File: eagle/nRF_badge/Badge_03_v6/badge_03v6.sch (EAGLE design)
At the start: 45 parts, among them J1 PROG_CONN_6, U1 LIS2DH12, U2 LP2985LV, U3 MCP6231, U5 M95M02, Y1 32768Hz

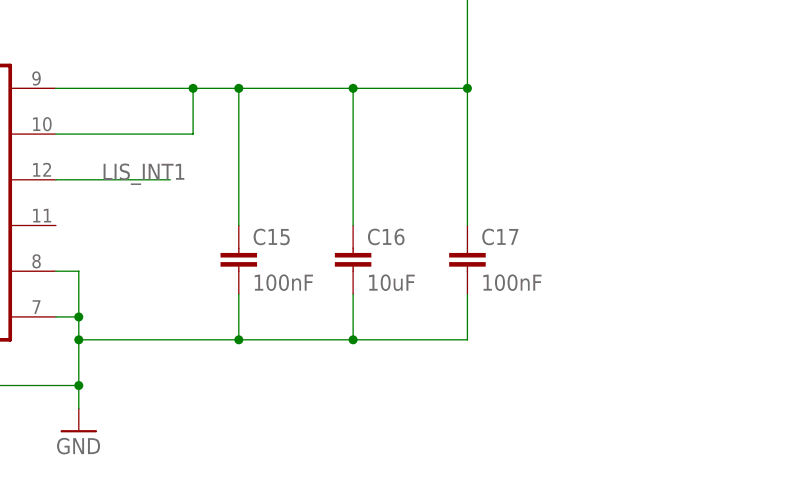
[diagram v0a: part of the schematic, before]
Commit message: Adding an accelerometer
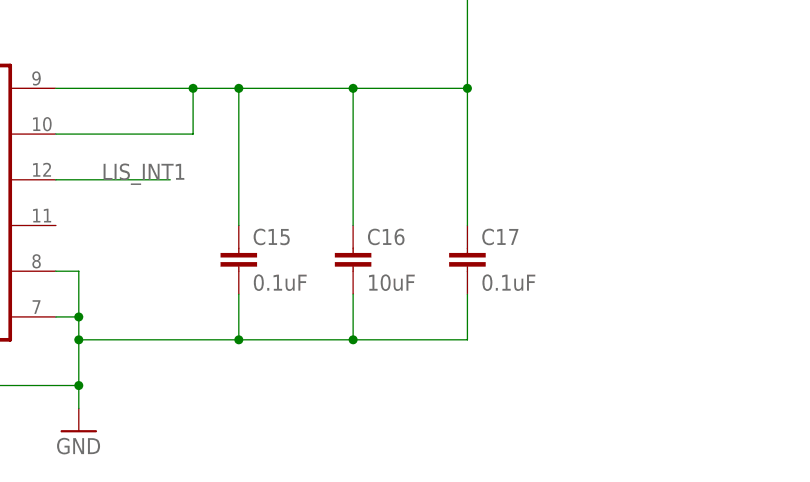
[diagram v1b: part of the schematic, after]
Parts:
- C15, C17: value 100nF -> 0.1uF
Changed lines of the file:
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@@
 <part name="GND9" library="Badge" deviceset="GND" device=""/>
 <part name="SUPPLY3" library="Badge" deviceset="VCC" device=""/>
-<part name="C15" library="rcl" deviceset="C-EU" device="C0603" value="100nF"/>
+<part name="C15" library="rcl" deviceset="C-EU" device="C0603" value="0.1uF"/>
 <part name="C16" library="rcl" deviceset="C-EU" device="C0603" value="10uF"/>
-<part name="C17" library="rcl" deviceset="C-EU" device="C0603" value="100nF"/>
+<part name="C17" library="rcl" deviceset="C-EU" device="C0603" value="0.1uF"/>
 <part name="SUPPLY18" library="Badge" deviceset="VCC" device=""/>
 <part name="SUPPLY19" library="Badge" deviceset="VCC" device=""/>

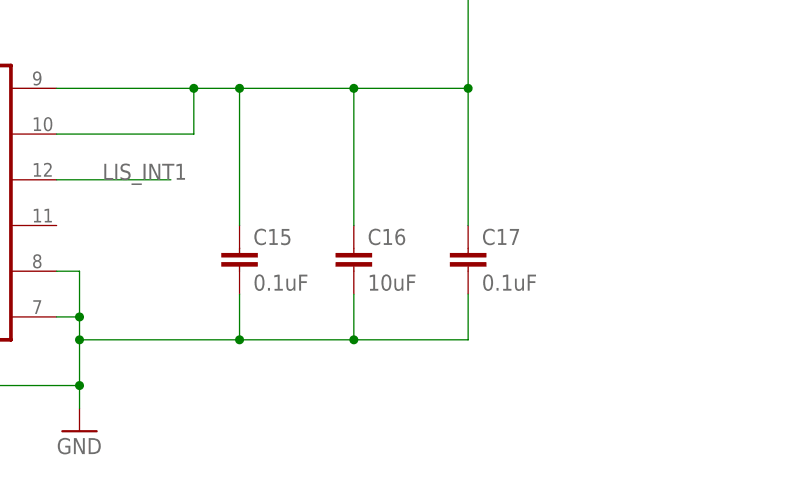
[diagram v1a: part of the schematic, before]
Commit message: Cleanning up labels
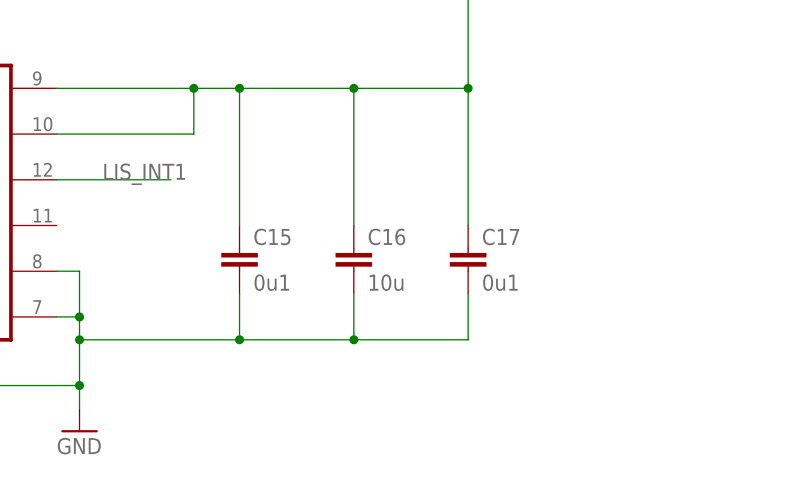
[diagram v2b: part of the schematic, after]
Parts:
- C15, C17: value 0.1uF -> 0u1
- C16: value 10uF -> 10u
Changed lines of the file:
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@@
 <part name="GND9" library="Badge" deviceset="GND" device=""/>
 <part name="SUPPLY3" library="Badge" deviceset="VCC" device=""/>
-<part name="C15" library="rcl" deviceset="C-EU" device="C0603" value="0.1uF"/>
-<part name="C16" library="rcl" deviceset="C-EU" device="C0603" value="10uF"/>
-<part name="C17" library="rcl" deviceset="C-EU" device="C0603" value="0.1uF"/>
+<part name="C15" library="rcl" deviceset="C-EU" device="C0603" value="0u1"/>
+<part name="C16" library="rcl" deviceset="C-EU" device="C0603" value="10u"/>
+<part name="C17" library="rcl" deviceset="C-EU" device="C0603" value="0u1"/>
 <part name="SUPPLY18" library="Badge" deviceset="VCC" device=""/>
 <part name="SUPPLY19" library="Badge" deviceset="VCC" device=""/>

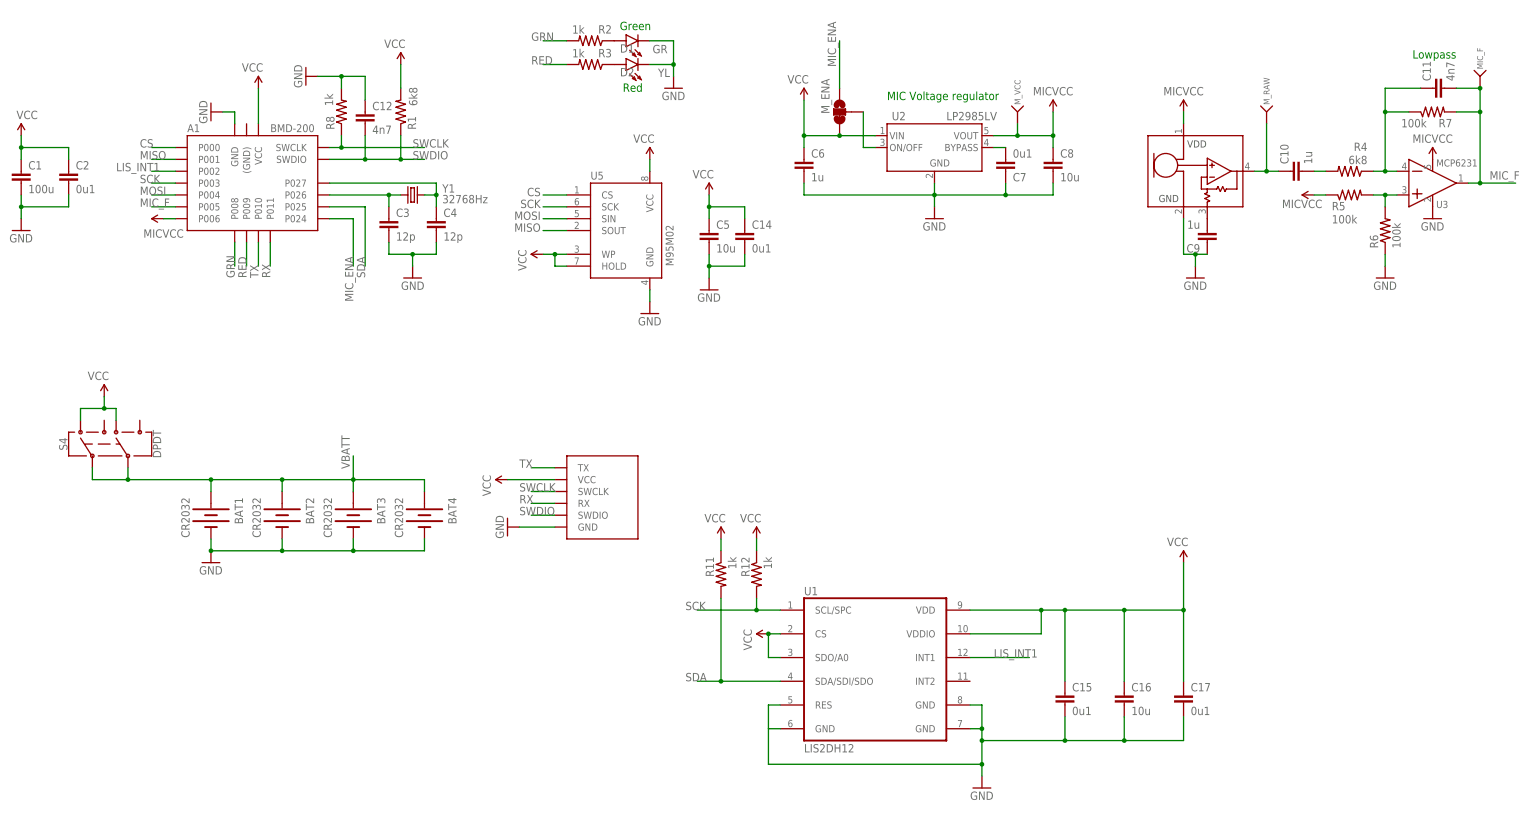
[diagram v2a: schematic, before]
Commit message: Re-routed LIS2DH12 to use SPI
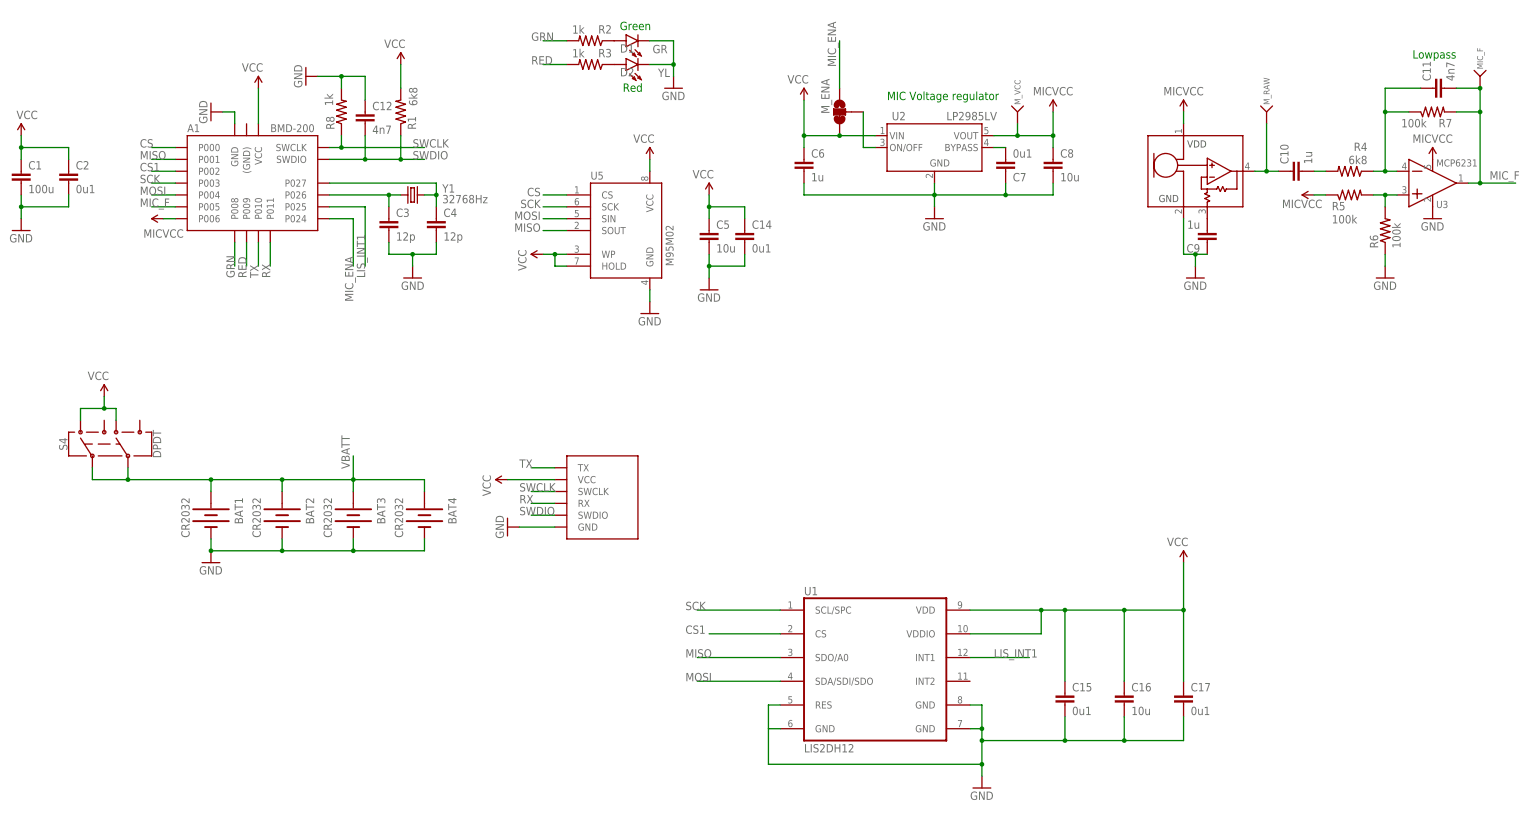
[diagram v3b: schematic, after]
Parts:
- removed R11, R12: 1k, rcl:R-US_R0603
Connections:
- removed net SDA: A1.P025, R11.2, U1.SDA/SDI/SDO
- new net CS1: A1.P002, U1.CS
- net LIS_INT1: now also A1.P025; no longer A1.P002
- net MISO: now also U1.SDO/A0
- net MOSI: now also U1.SDA/SDI/SDO
- net SCK: no longer R12.2
- net VCC: no longer R11.1, R12.1, U1.CS, U1.SDO/A0
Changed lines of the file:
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@@
 <part name="SUPPLY15" library="Badge" deviceset="VCC" device=""/>
 <part name="GND9" library="Badge" deviceset="GND" device=""/>
-<part name="SUPPLY3" library="Badge" deviceset="VCC" device=""/>
 <part name="C15" library="rcl" deviceset="C-EU" device="C0603" value="0u1"/>
 <part name="C16" library="rcl" deviceset="C-EU" device="C0603" value="10u"/>
 <part name="C17" library="rcl" deviceset="C-EU" device="C0603" value="0u1"/>
 <part name="SUPPLY18" library="Badge" deviceset="VCC" device=""/>
-<part name="SUPPLY19" library="Badge" deviceset="VCC" device=""/>
-<part name="SUPPLY20" library="Badge" deviceset="VCC" device=""/>
-<part name="R11" library="rcl" deviceset="R-US_" device="R0603" value="1k"/>
-<part name="R12" library="rcl" deviceset="R-US_" device="R0603" value="1k"/>
 <part name="U1" library="Badge" deviceset="LIS2DH12" device=""/>
 </parts>
@@
 <instance part="SUPPLY15" gate="G$1" x="12.7" y="43.18" rot="MR0"/>
 <instance part="GND9" gate="1" x="200.66" y="-40.64"/>
-<instance part="SUPPLY3" gate="G$1" x="154.94" y="-7.62" rot="MR270"/>
 <instance part="C15" gate="G$1" x="218.44" y="-20.32"/>
 <instance part="C16" gate="G$1" x="231.14" y="-20.32"/>
 <instance part="C17" gate="G$1" x="243.84" y="-20.32"/>
 <instance part="SUPPLY18" gate="G$1" x="243.84" y="7.62" rot="MR0"/>
-<instance part="SUPPLY19" gate="G$1" x="152.4" y="12.7" rot="MR0"/>
-<instance part="SUPPLY20" gate="G$1" x="144.78" y="12.7" rot="MR0"/>
-<instance part="R11" gate="G$1" x="144.78" y="5.08" rot="MR270"/>
-<instance part="R12" gate="G$1" x="152.4" y="5.08" rot="MR270"/>
 <instance part="U1" gate="G$1" x="177.8" y="-15.24"/>
 </instances>
@@
 </segment>
 <segment>
-<pinref part="SUPPLY3" gate="G$1" pin="VCC"/>
-<wire x1="157.48" y1="-7.62" x2="154.94" y2="-7.62" width="0.1524" layer="91"/>
-<pinref part="U1" gate="G$1" pin="CS"/>
-<pinref part="U1" gate="G$1" pin="SDO/A0"/>
-<wire x1="157.48" y1="-12.7" x2="154.94" y2="-12.7" width="0.1524" layer="91"/>
-<wire x1="154.94" y1="-12.7" x2="154.94" y2="-7.62" width="0.1524" layer="91"/>
-<junction x="154.94" y="-7.62"/>
-</segment>
-<segment>
 <wire x1="198.12" y1="-7.62" x2="213.36" y2="-7.62" width="0.1524" layer="91"/>
 <wire x1="198.12" y1="-2.54" x2="213.36" y2="-2.54" width="0.1524" layer="91"/>
@@
 <pinref part="U1" gate="G$1" pin="VDDIO"/>
 </segment>
-<segment>
-<pinref part="SUPPLY20" gate="G$1" pin="VCC"/>
-<pinref part="R11" gate="G$1" pin="1"/>
-<wire x1="144.78" y1="12.7" x2="144.78" y2="10.16" width="0.1524" layer="91"/>
-</segment>
-<segment>
-<pinref part="SUPPLY19" gate="G$1" pin="VCC"/>
-<pinref part="R12" gate="G$1" pin="1"/>
-<wire x1="152.4" y1="12.7" x2="152.4" y2="10.16" width="0.1524" layer="91"/>
-</segment>
 </net>
 <net name="SCK" class="0">
@@
 </segment>
 <segment>
-<wire x1="157.48" y1="-2.54" x2="152.4" y2="-2.54" width="0.1524" layer="91"/>
-<pinref part="R12" gate="G$1" pin="2"/>
-<wire x1="152.4" y1="-2.54" x2="139.7" y2="-2.54" width="0.1524" layer="91"/>
-<wire x1="152.4" y1="0" x2="152.4" y2="-2.54" width="0.1524" layer="91"/>
-<junction x="152.4" y="-2.54"/>
+<wire x1="157.48" y1="-2.54" x2="139.7" y2="-2.54" width="0.1524" layer="91"/>
 <label x="137.16" y="-2.54" size="1.778" layer="95"/>
 <pinref part="U1" gate="G$1" pin="SCL/SPC"/>
@@
 <label x="20.32" y="86.36" size="1.778" layer="95"/>
 </segment>
+<segment>
+<wire x1="157.48" y1="-17.78" x2="139.7" y2="-17.78" width="0.1524" layer="91"/>
+<label x="137.16" y="-17.78" size="1.778" layer="95"/>
+<pinref part="U1" gate="G$1" pin="SDA/SDI/SDO"/>
+</segment>
 </net>
 <net name="MISO" class="0">
@@
 <wire x1="27.94" y1="93.98" x2="22.86" y2="93.98" width="0.1524" layer="91"/>
 <label x="20.32" y="93.98" size="1.778" layer="95"/>
+</segment>
+<segment>
+<pinref part="U1" gate="G$1" pin="SDO/A0"/>
+<wire x1="157.48" y1="-12.7" x2="139.7" y2="-12.7" width="0.1524" layer="91"/>
+<label x="137.16" y="-12.7" size="1.778" layer="95"/>
 </segment>
 </net>
@@
 </segment>
 </net>
-<net name="SDA" class="0">
+<net name="CS" class="0">
+<segment>
+<pinref part="A1" gate="G$1" pin="P000"/>
+<wire x1="27.94" y1="96.52" x2="22.86" y2="96.52" width="0.1524" layer="91"/>
+<label x="20.32" y="96.52" size="1.778" layer="95"/>
+</segment>
+<segment>
+<wire x1="111.76" y1="86.36" x2="106.68" y2="86.36" width="0.1524" layer="91"/>
+<label x="106.172" y="87.884" size="1.778" layer="95" rot="R180"/>
+<pinref part="U5" gate="G$1" pin="CS"/>
+</segment>
+</net>
+<net name="LIS_INT1" class="0">
+<segment>
+<wire x1="198.12" y1="-12.7" x2="210.82" y2="-12.7" width="0.1524" layer="91"/>
+<pinref part="U1" gate="G$1" pin="INT1"/>
+<label x="203.2" y="-12.7" size="1.778" layer="95"/>
+</segment>
 <segment>
 <wire x1="68.58" y1="83.82" x2="68.58" y2="71.12" width="0.1524" layer="91"/>
@@
 <wire x1="68.58" y1="83.82" x2="60.96" y2="83.82" width="0.1524" layer="91"/>
 </segment>
-<segment>
-<wire x1="157.48" y1="-17.78" x2="144.78" y2="-17.78" width="0.1524" layer="91"/>
-<pinref part="R11" gate="G$1" pin="2"/>
-<wire x1="144.78" y1="-17.78" x2="139.7" y2="-17.78" width="0.1524" layer="91"/>
-<wire x1="144.78" y1="0" x2="144.78" y2="-17.78" width="0.1524" layer="91"/>
-<junction x="144.78" y="-17.78"/>
-<label x="137.16" y="-17.78" size="1.778" layer="95"/>
-<pinref part="U1" gate="G$1" pin="SDA/SDI/SDO"/>
-</segment>
-</net>
-<net name="CS" class="0">
-<segment>
-<pinref part="A1" gate="G$1" pin="P000"/>
-<wire x1="27.94" y1="96.52" x2="22.86" y2="96.52" width="0.1524" layer="91"/>
-<label x="20.32" y="96.52" size="1.778" layer="95"/>
-</segment>
-<segment>
-<wire x1="111.76" y1="86.36" x2="106.68" y2="86.36" width="0.1524" layer="91"/>
-<label x="106.172" y="87.884" size="1.778" layer="95" rot="R180"/>
-<pinref part="U5" gate="G$1" pin="CS"/>
-</segment>
-</net>
-<net name="LIS_INT1" class="0">
-<segment>
-<wire x1="198.12" y1="-12.7" x2="210.82" y2="-12.7" width="0.1524" layer="91"/>
-<pinref part="U1" gate="G$1" pin="INT1"/>
-<label x="203.2" y="-12.7" size="1.778" layer="95"/>
-</segment>
+</net>
+<net name="CS1" class="0">
 <segment>
 <pinref part="A1" gate="G$1" pin="P002"/>
 <wire x1="27.94" y1="91.44" x2="22.86" y2="91.44" width="0.1524" layer="91"/>
-<label x="15.24" y="91.44" size="1.778" layer="95"/>
-</segment>
-</net>
+<label x="20.32" y="91.44" size="1.778" layer="95"/>
+</segment>
+<segment>
+<pinref part="U1" gate="G$1" pin="CS"/>
+<wire x1="157.48" y1="-7.62" x2="142.24" y2="-7.62" width="0.1524" layer="91"/>
+<label x="137.16" y="-7.62" size="1.778" layer="95"/>
+</segment>
+</net>
